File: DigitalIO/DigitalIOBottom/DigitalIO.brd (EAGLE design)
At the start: 64 x 82 mm, 75 parts, among them IC1 MCP23017SP, IC2 ULN2803A, K5 HF46105, K6 HF46105, K7 HF46105, K8 HF46105, P1 DF11-06-2DS, Q1 BS170, Q2 BS170, Q3 BS170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

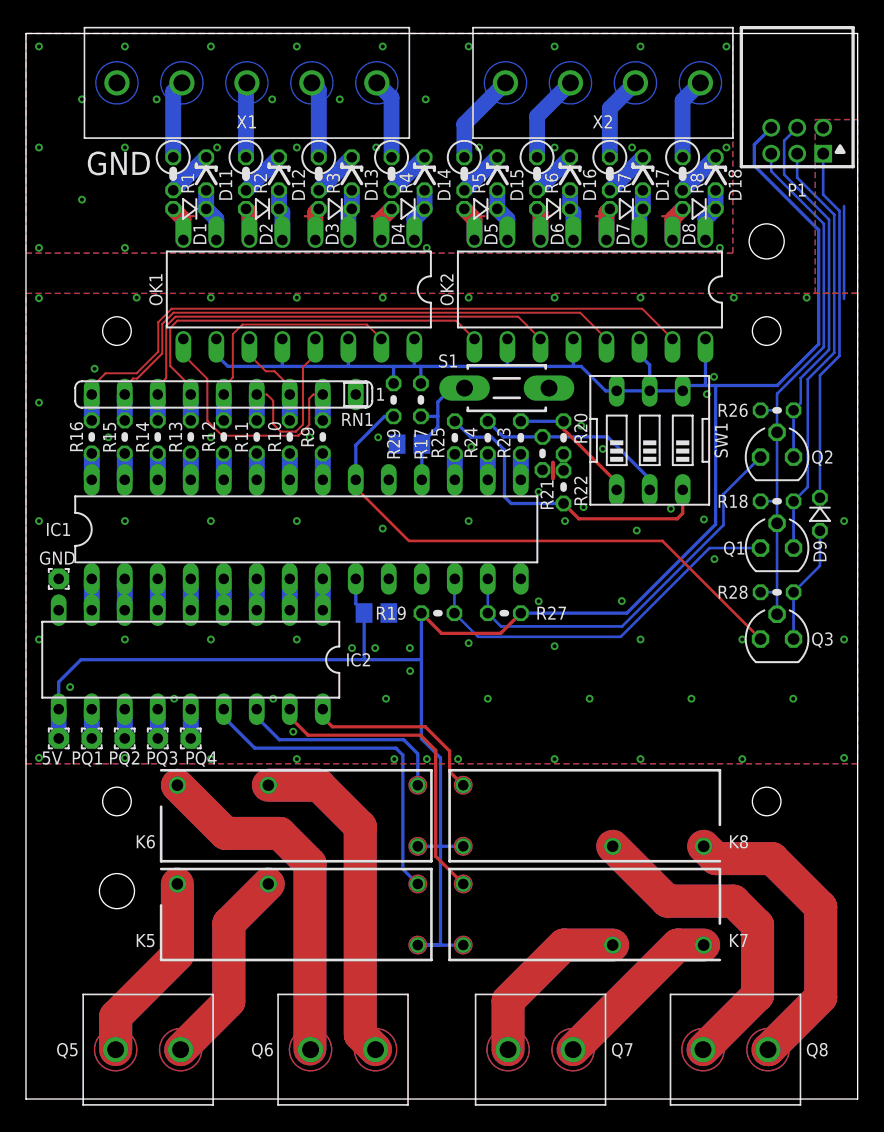
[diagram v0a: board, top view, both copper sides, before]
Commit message: Rework to operate with 5V only. Add INT and RESET signals.
Signed-off-by: Alexander Falkenstern <alexander.falkenstern@gmail.com>
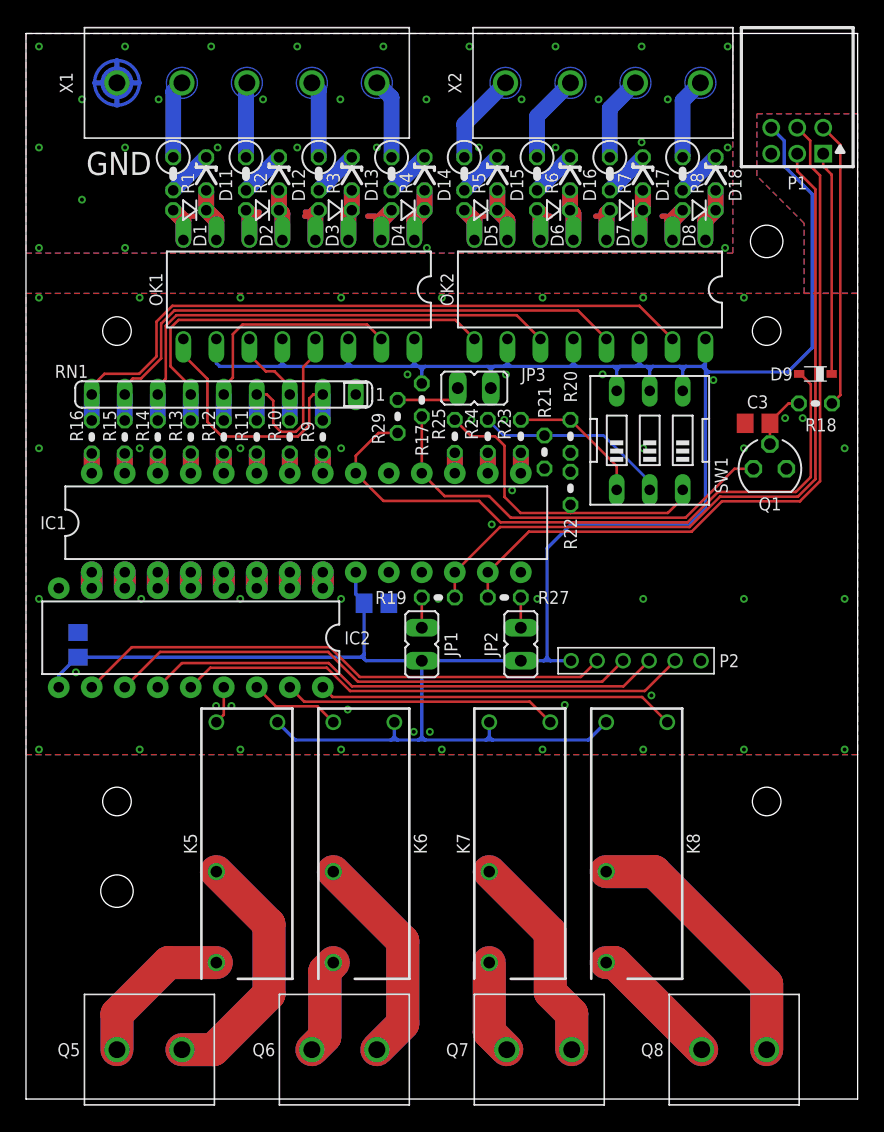
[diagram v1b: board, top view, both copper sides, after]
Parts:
- removed 5V, GND, PQ1, PQ2, PQ3, PQ4: WIREPAD1,6/0,8, wirepad:1,6/0,8
- removed Q2, Q3: BS170, transistor-small-signal:SOT54E
- removed R26, R28: 1K, rcl:0204V
- removed S1: DTS-3, switch-tact:DTS-3
- added C3: 100nF, rcl:C0805
- added JP1, JP2, JP3: (no value), jumper:JP1
- added P2: (no value), Board_to_Board_Connectors_rev15d:62000611121
- D1, D2, D3, D4, D5, D6, D7, D8: value 1N4148DO35-2V -> 1N4148
- D9: value 1N4148DO35-2V -> BAT60A; device diode:DO35-2V -> diode:SOD323_ST
- IC1: value MCP23017SP -> MCP23017SP2; device mcp:DIL28-3 -> mcp:DIL28-3-ROUND
- IC2: device uln-udn:DIL18 -> uln-udn:DIL18-ROUND
- R18: value 1K -> 100R; device rcl:0204V -> resistor:0204V
- R29: value 1K -> 10K
- moved C2 29.8 mm to (4.00, 35.0), turned to 270 degrees
- moved D9 10.8 mm to (60.8, 55.8), turned to 180 degrees
- moved R18 8.09 mm to (60.8, 53.5)
- moved K7 7.40 mm to (38.0, 19.6), turned to 270 degrees
- moved K5 6.64 mm to (17.0, 19.6), turned to 270 degrees
- moved Q1 6.12 mm to (57.2, 48.5)
- moved K6 5.63 mm to (26.0, 19.6), turned to 270 degrees
- moved K8 4.54 mm to (47.0, 19.6), turned to 270 degrees
- moved IC2 1.69 mm to (12.7, 35.5)
- moved R29 1.31 mm to (28.6, 52.5)
- moved R19 1.21 mm to (31.7, 38.6)
- moved R27 1.21 mm to (36.8, 38.6), turned to 180 degrees
- moved C1 0.75 mm to (27.0, 38.1)
- moved R20 0.54 mm to (41.9, 51.0), turned to 270 degrees
- moved R22 0.54 mm to (41.9, 47.0), turned to 90 degrees
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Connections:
- removed net +3V3: P1.5, Q1.G, Q2.G, Q3.G, R18.2, R26.2, R28.2
- removed net N$57: C2.2, IC1.18, R17.1, S1.2
- removed net N$81: IC1.20, Q3.D, R29.2
- new net INT: D9.A, IC1.20, R29.2
- new net RESET: IC1.18, Q1.D, R17.2
- new net SCL: IC1.12, P1.3, R19.2
- new net SDA: IC1.13, P1.4, R27.2
- net +5V: now also C2.2, JP1.1, JP2.1, JP3.1, P2.1, R17.1; no longer 5V.1, R17.2, R19.1, R27.2, R29.1
- net GND: now also C3.1, P1.5, P2.6, Q1.S, R20.2, R21.2, R22.2; no longer GND.1, P1.2, R20.1, R21.1, R22.1, S1.1
- net N$11: now also R22.1, R25.2; no longer R22.2, R25.1
- net N$28: now also P2.5; no longer PQ4.1
- net N$30: now also P2.4; no longer PQ3.1
- net N$32: now also P2.3; no longer PQ2.1
- net N$34: now also P2.2; no longer PQ1.1
- net N$36: now also JP2.2, R27.1; no longer D9.A, Q3.S, R28.1
- net N$50: now also R23.1; no longer R23.2
- net N$52: now also R24.1; no longer R24.2
- net N$58: now also JP3.2, R29.1; no longer IC1.12, Q1.D, R19.2
- net N$61: now also JP1.2, R19.1; no longer IC1.13, Q2.D, R27.1
- net N$69: now also P1.2, R18.1; no longer P1.4, Q2.S, R26.1
- net N$71: now also C3.2, Q1.G, R18.2; no longer P1.3, Q1.S, R18.1
- net N$77: now also R20.1, R23.2; no longer R20.2, R23.1
- net N$78: now also R21.1, R24.2; no longer R21.2, R24.1
- net N$79: now also R25.1; no longer R25.2
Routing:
- net SDA: track 0.00 -> 58.4 mm
- net SCL: track 0.00 -> 58.3 mm
- net INT: track 0.00 -> 51.7 mm
- net N$81: track 43.1 -> 0.00 mm
- net +3V3: track 42.4 -> 0.00 mm
- net N$34: track 2.25 -> 41.6 mm
- net N$88: track 53.9 -> 14.8 mm
- net N$32: track 2.25 -> 41.1 mm
- net N$30: track 2.25 -> 40.1 mm
- net N$28: track 2.25 -> 39.6 mm
- net RESET: track 0.00 -> 32.9 mm
- net N$61: track 30.8 -> 2.33 mm
- net N$71: track 32.8 -> 4.52 mm
- net N$38: track 47.2 -> 20.3 mm
- net N$58: track 29.8 -> 5.29 mm
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- removed copper zone on layer 1, net +5V
- removed copper zone on layer 16, net +5V
- removed copper zone on layer 1, net N$38
- removed copper zone on layer 16, net N$38
- removed copper zone on layer 1, net N$40
- removed copper zone on layer 16, net N$40
- removed copper zone on layer 1, net N$42
- removed copper zone on layer 16, net N$42
- removed copper zone on layer 1, net N$44
- removed copper zone on layer 16, net N$44
- removed copper zone on layer 1, net N$46
- removed copper zone on layer 16, net N$46
- removed copper zone on layer 1, net N$48
- removed copper zone on layer 16, net N$48
- removed copper zone on layer 1, net N$54
- removed copper zone on layer 16, net N$54
- removed copper zone on layer 1, net N$56
- removed copper zone on layer 16, net N$56
- removed copper zone on layer 1, net N$66
- removed copper zone on layer 16, net N$66
- removed copper zone on layer 1, net N$75
- removed copper zone on layer 16, net N$75
- removed copper zone on layer 1, net N$88
- removed copper zone on layer 16, net N$88
- removed copper zone on layer 1, net N$89
- removed copper zone on layer 16, net N$89
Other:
- board text added: "8DI/8DO V1.1"
- board text added: "INT"
- board text added: "JP1/SCL, JP2/SDA: Pull high, if set JP3/INT: Set, if open drain"
- board text added: "P1"
- board text added: "RESET"
- board text removed: "3.3V"
- board text removed: "8DI/8DO"
- board text removed: "INT-Settings: 1. Mirror 2. Open drain"
- board text removed: "INT/NC"
